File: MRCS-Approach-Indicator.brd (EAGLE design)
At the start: 99.8 x 68.8 mm, 21 parts, among them J1 5 VDC, J2 Output, J3 Station 0, J4 Station 1, J5 Stations 2 and 3, J6 relay out, K1 G6H2-100, K2 G6H2-100, K3 G6H2-100, K4 G6H2-100

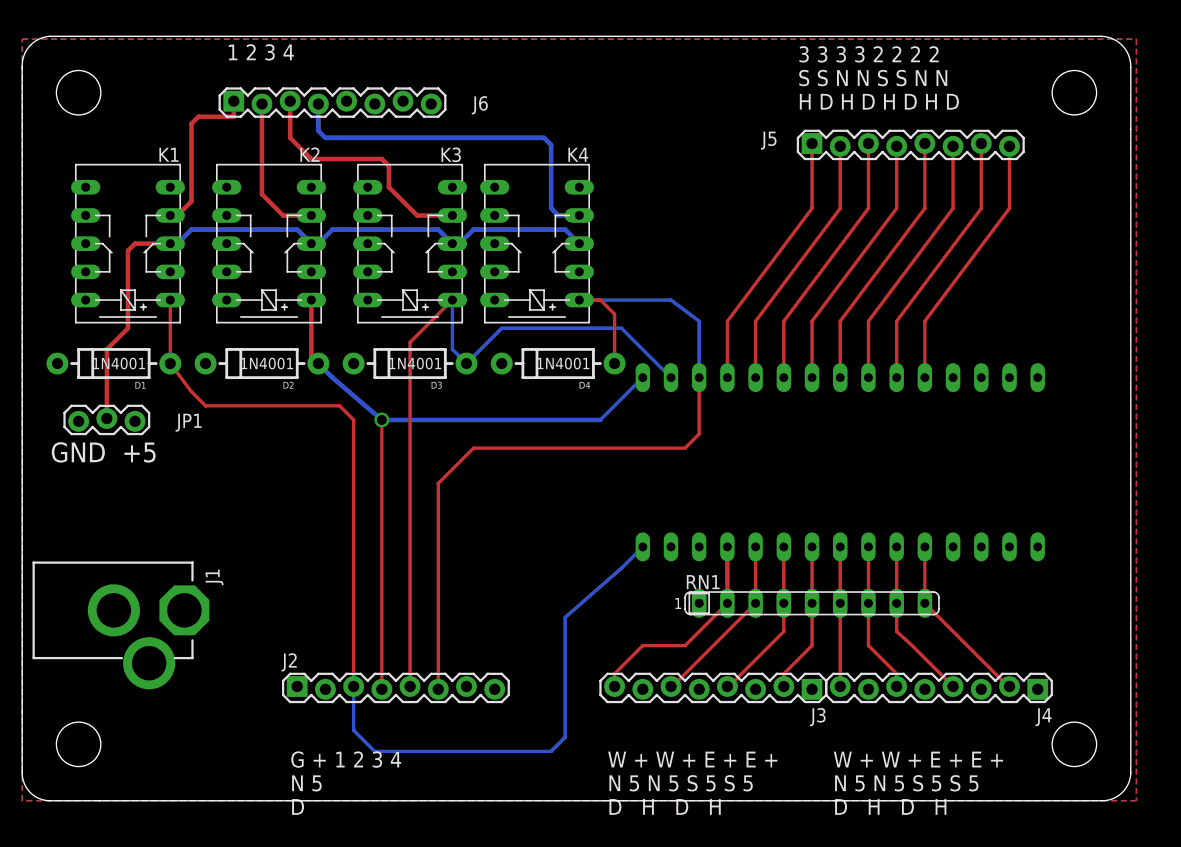
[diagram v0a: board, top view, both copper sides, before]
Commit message: changes after design review
- changed contacts to dry pairs with grounding jumper
- added LEDs for relay status
- re-arranged raw logic outputs and added another +5/GND pair
- fixed label issues
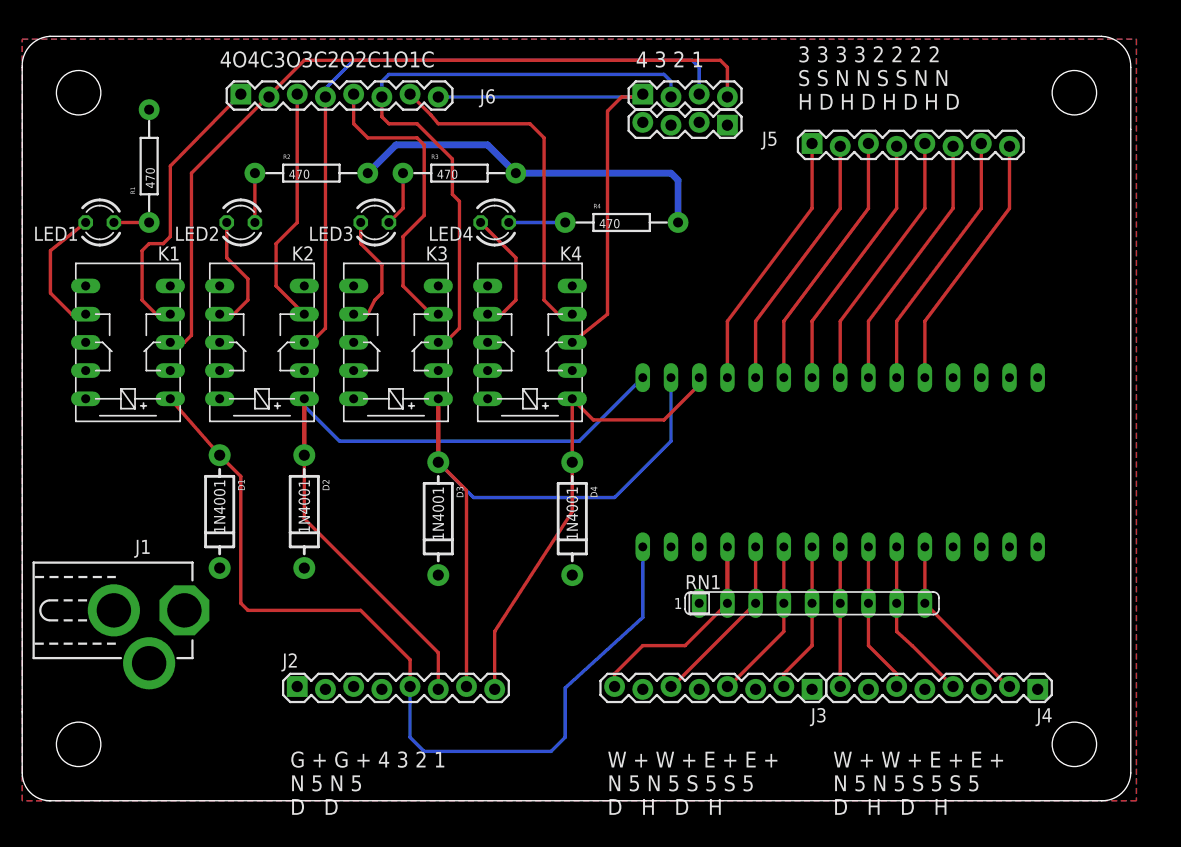
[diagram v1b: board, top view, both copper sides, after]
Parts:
- removed JP1: output polarity, SPCoast:1X03
- added CON1: GND, SPCoast:1X04_LOCK
- added CON2: GND Jumpers, SPCoast:1X04_LOCK
- added LED1, LED2, LED3, LED4: RED, SPCoast:LED3MM
- added R1, R2, R3, R4: 470, SPCoast:AXIAL-0.4-RES
- moved D1 16.4 mm to (17.8, 26.0), turned to 90 degrees
- moved D3 14.2 mm to (37.5, 25.4), turned to 90 degrees
- moved D4 14.0 mm to (49.5, 25.4), turned to 90 degrees
- moved D2 13.9 mm to (25.4, 26.0), turned to 90 degrees
- moved K3 8.98 mm to (33.7, 41.3)
- moved K2 8.91 mm to (21.6, 41.3)
- moved K4 8.91 mm to (45.7, 41.3)
- moved K1 8.89 mm to (9.53, 41.3)
- moved J6 0.90 mm to (19.7, 63.5)
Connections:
- removed net D11: D3.A, J2.5, K3.1, NANO.D11
- new net N$1: J6.3, K2.S1
- new net N$24: J6.7, K4.S1
- new net N$25: CON2.1, J6.8, K4.P1
- new net N$26: K1.S2, LED1.K
- new net N$27: LED1.A, R1.P$1
- new net N$28: LED2.A, R2.P$1
- new net N$29: K2.S2, LED2.K
- new net N$30: LED3.A, R3.P$1
- new net N$31: K3.S2, LED3.K
- new net N$32: LED4.A, R4.P$1
- new net N$33: K4.S2, LED4.K
- new net N$34: D3.A, J2.7, K3.1, NANO.D11
- net 5V: now also J2.4, R1.P$2, R2.P$2, R3.P$2, R4.P$2; no longer JP1.3
- net D12: now also J2.6; no longer J2.4
- net D7: now also J2.5; no longer J2.3
- net GND: now also CON1.1, CON1.2, CON1.3, CON1.4, J2.3, K1.P2, K2.P2, K3.P2, K4.P2; no longer JP1.1
- net N$2: now also J2.8; no longer J2.6
- net N$21: now also J6.5; no longer J6.3
- net N$22: now also CON2.4, J6.2, K1.P1; no longer J6.4, K4.S1
- net N$23: now also CON2.2, J6.6; no longer JP1.2, K1.P1, K2.P1, K4.P1
- net N$8: now also CON2.3, J6.4, K2.P1; no longer J6.2, K2.S1
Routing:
- net D11: track 64.2 -> 0.00 mm
- net N$34: track 0.00 -> 57.8 mm
- net N$8: track 13.4 -> 61.4 mm
- net N$25: track 0.00 -> 44.7 mm
- net N$22: track 32.4 -> 72.2 mm
- net 5V: track 0.00 -> 34.1 mm
- net N$24: track 0.00 -> 31.4 mm
- net N$2: track 73.6 -> 42.3 mm
- net N$1: track 0.00 -> 21.7 mm
- net D7: track 93.1 -> 80.5 mm
- net N$33: track 0.00 -> 12.0 mm
- net N$26: track 0.00 -> 11.8 mm
- net N$31: track 0.00 -> 11.4 mm
- net N$7: track 14.9 -> 26.0 mm
- net N$29: track 0.00 -> 10.8 mm
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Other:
- board text added: "4 3 2 1"
- board text added: "4O4C3O3C2O2C1O1C"
- board text added: "G + G + 4 3 2 1 N 5 N 5 D D"
- board text added: "V1.0 20210828"
- board text removed: "1 2 3 4"
- board text removed: "G + 1 2 3 4 N 5 D"
- board text removed: "GND +5"
- board text removed: "V1.0 20210827"

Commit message: Order as submitter to JLCPCB
Changes after design review with Jon Schmidt, various label clean up items.  Thanks to John Plocher for suggestions on managing back side labels and logos!
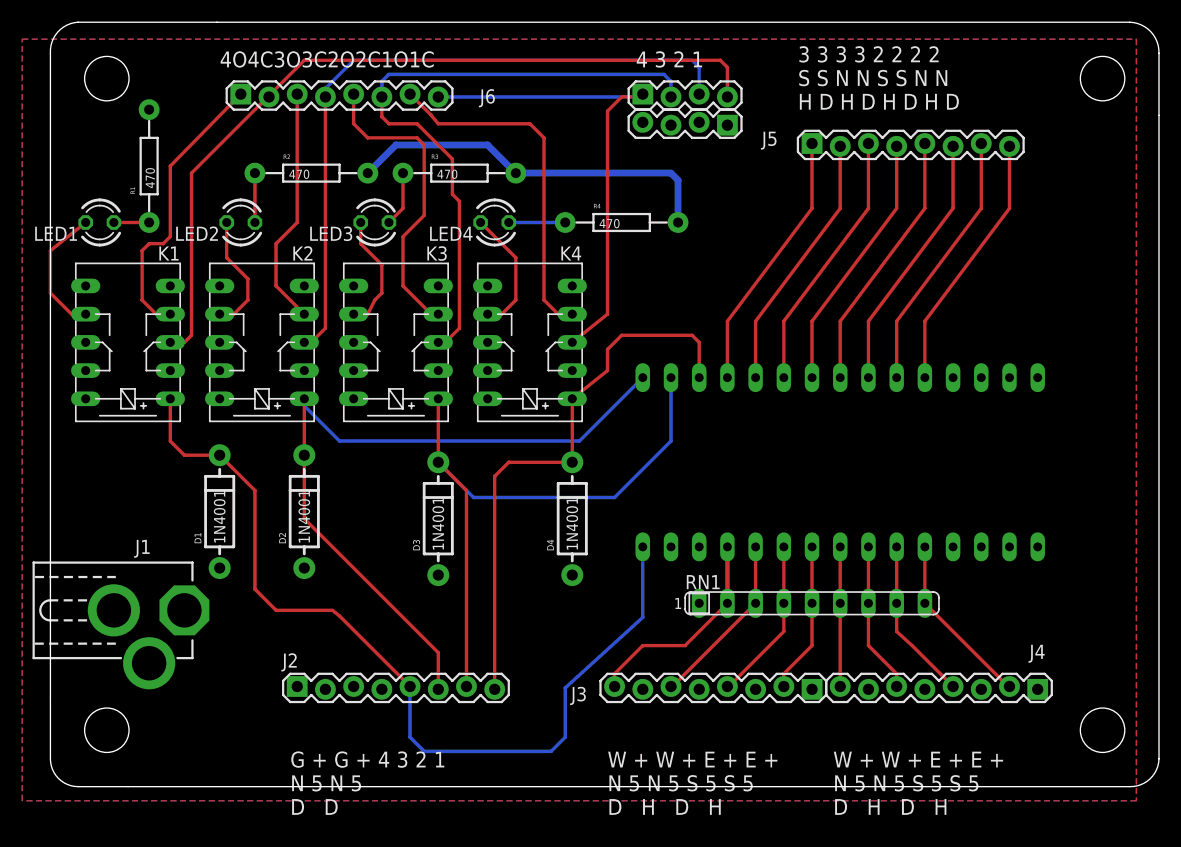
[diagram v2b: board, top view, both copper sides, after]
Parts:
- moved U$5 25.5 mm to (78.1, 27.9)
- moved U$3 14.9 mm to (5.71, 25.4)
- moved U$1 2.84 mm to (2.54, 1.27)
- turned D1 to 270 degrees
- turned D2 to 270 degrees
- turned D3 to 270 degrees
- turned D4 to 270 degrees
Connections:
- net D12: now also D2.C; no longer D2.A
- net D7: now also D1.C; no longer D1.A
- net GND: now also D1.A, D2.A, D3.A, D4.A; no longer D1.C, D2.C, D3.C, D4.C
- net N$2: now also D4.C; no longer D4.A
- net N$34: now also D3.C; no longer D3.A
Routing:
- net N$2: track 42.3 -> 50.6 mm
- net D7: track 80.5 -> 79.6 mm
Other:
- board text removed: "BRN ORN"
